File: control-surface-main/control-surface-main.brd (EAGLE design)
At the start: 105.5 x 54.1 mm, 81 parts, among them IC1 74HC595D, IC2 4051D, IC3 4051D

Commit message: in work
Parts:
- added C2, C3: (no value), rcl:C0805
- moved C1 16.9 mm to (91.4, 34.3), turned to 90 degrees
- moved K6 4.58 mm to (109.2, 12.7)
- moved KR5 4.58 mm to (109.2, 22.9)
- moved CLK_OUT 4.58 mm to (109.2, 5.08)
- moved K4 4.58 mm to (109.2, 15.2)
- moved KR7 4.58 mm to (109.2, 10.2)
- moved DAT_OUT 4.58 mm to (109.2, 7.62)
- moved K0 4.58 mm to (109.2, 20.3)
- moved K2 4.58 mm to (109.2, 17.8)
- moved K7 4.58 mm to (106.7, 12.7)
- moved KR13 4.58 mm to (106.7, 22.9)
- moved GND5 4.58 mm to (106.7, 5.08)
- moved K5 4.58 mm to (106.7, 15.2)
- moved KR6 4.58 mm to (106.7, 10.2)
- moved OE_OUT 4.58 mm to (106.7, 7.62)
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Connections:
- net GND: now also C2.2, C3.2
- net VCC: now also C2.1, C3.1
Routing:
- net DAT_IN: track 179.9 -> 142.8 mm
- net KSA: track 203.1 -> 183.3 mm
- net N$38: track 97.4 -> 85.5 mm
- net N$12: track 102.1 -> 113.9 mm
- net N$23: track 75.6 -> 64.1 mm
- net N$13: track 91.6 -> 102.1 mm
- net N$14: track 76.0 -> 85.7 mm
- net N$1: track 126.2 -> 135.4 mm
- net N$15: track 62.0 -> 71.1 mm
- net GND: track 134.6 -> 142.3 mm, vias 2 -> 5
- net N$16: track 46.0 -> 53.1 mm
- net N$19: track 116.5 -> 112.1 mm
- net N$32: track 65.5 -> 61.9 mm
- net N$35: track 63.8 -> 60.5 mm
- net N$11: track 36.1 -> 39.3 mm
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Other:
- board size 105.5 x 54.1 mm -> 102.9 x 54.1 mm

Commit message: mode mods
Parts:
- moved R7 2.54 mm to (40.6, 6.35)
- moved LED7 2.12 mm to (46.1, 5.08)
- moved R5 1.27 mm to (61.0, 6.35)
- moved LED5 0.42 mm to (66.9, 5.08)
- turned KCK to 0 degrees
- turned RD1 to 90 degrees
- renumbered ANA0 to RD0, ANA1 to KCK, CLK_IN to LCK, DAT_IN to DAT, GND to 0V, KS_CLK to RD1, OE_IN to LOE, SELA to A, SELB to B, SELC to C, VCC to 5V
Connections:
- net N$19: now also KCK.1; no longer RD1.1
- net N$45: now also RD1.1; no longer KCK.1
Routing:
- net N$45: track 51.3 -> 48.4 mm, vias 2 -> 1
- net N$31: track 33.9 -> 31.4 mm
- net VCC: track 181.4 -> 183.4 mm
- net N$29: track 55.0 -> 53.8 mm
- net N$19: track 112.1 -> 113.2 mm
- net N$24: track 4.13 -> 4.98 mm

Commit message: stuff
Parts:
- renumbered LED5 to LED3, LED6 to LED4, LED7 to LED2, LED8 to LED1, U$1 to D6, U$2 to D7, U$3 to D8, U$4 to D1, U$5 to D2, U$6 to D3, U$7 to D4, U$8 to D5
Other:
- board text added: "KEYS/LEDS"
- board text added: "POTS SCAN"

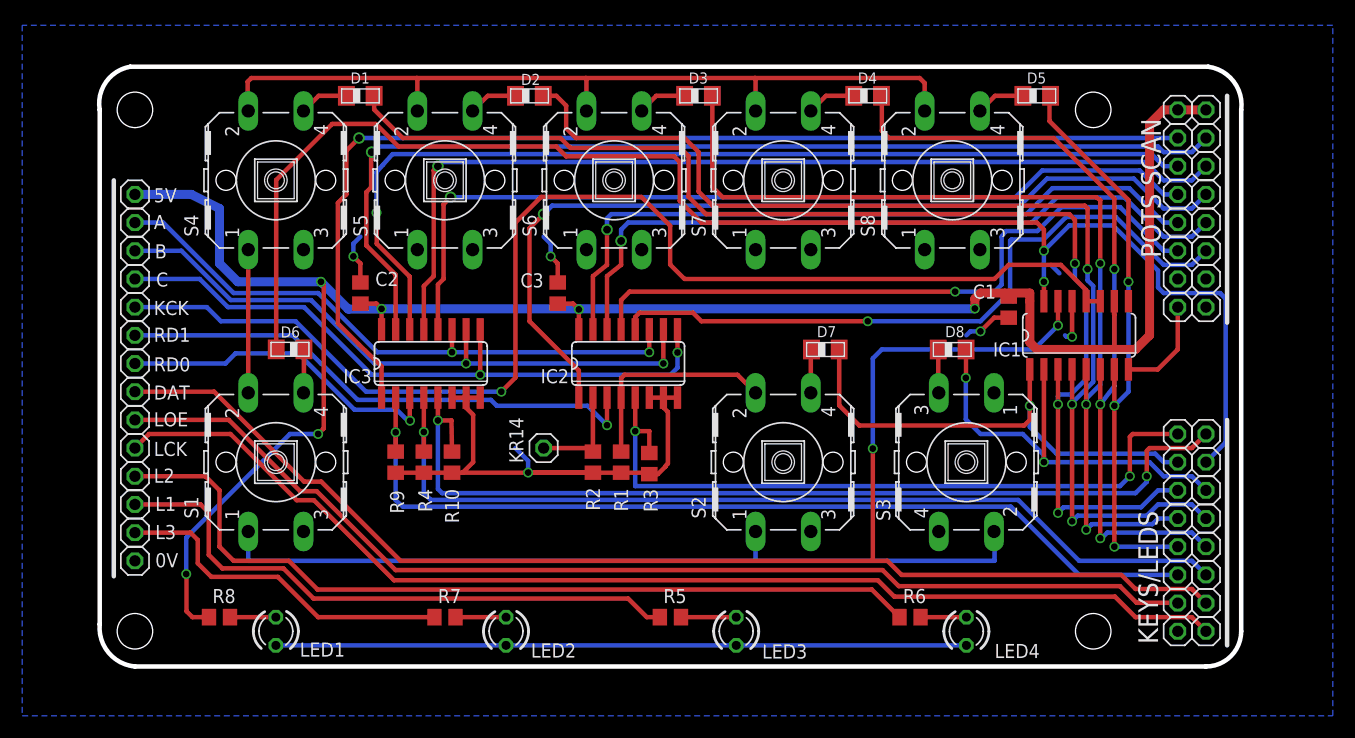
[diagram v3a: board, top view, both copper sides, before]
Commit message: move leds
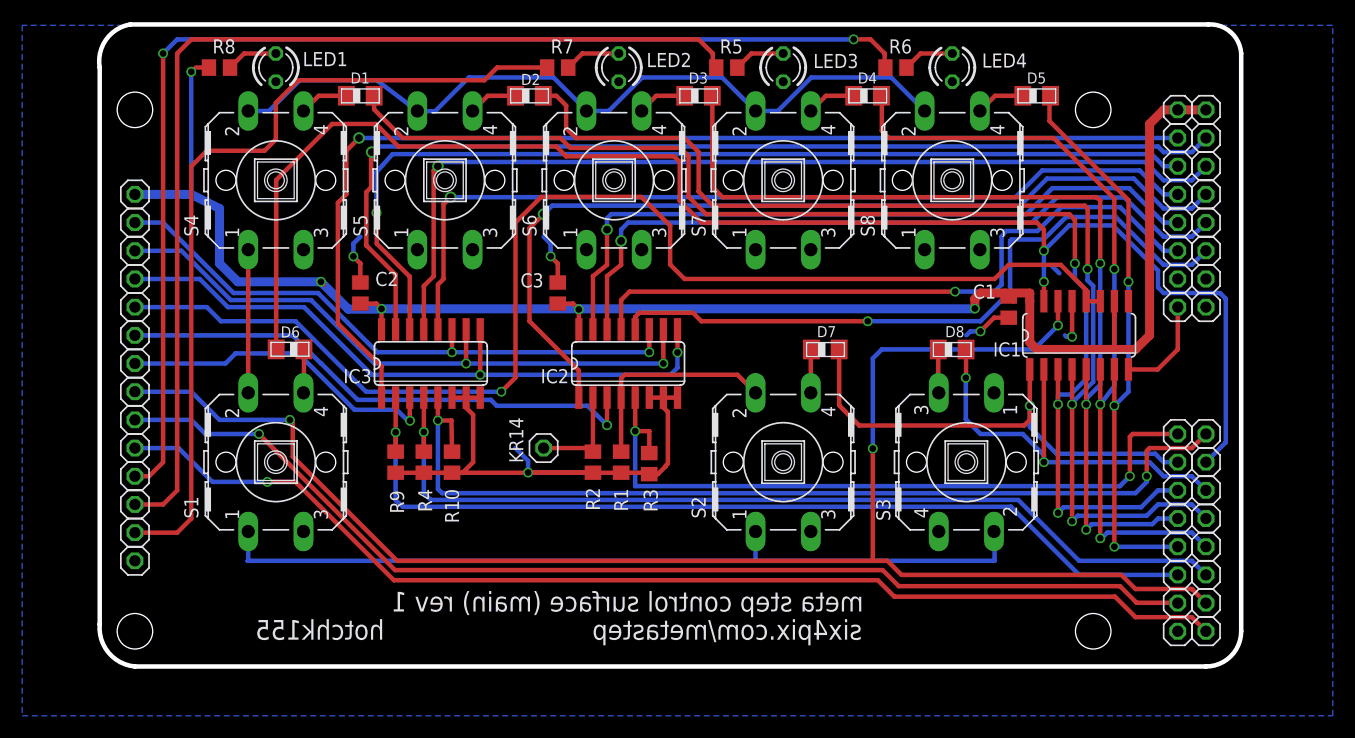
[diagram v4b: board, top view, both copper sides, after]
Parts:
- moved LED2 51.8 mm to (56.3, 55.9)
- moved LED3 51.0 mm to (71.1, 55.9)
- moved LED4 50.8 mm to (86.4, 55.9)
- moved LED1 50.8 mm to (25.4, 55.9)
- moved R7 50.6 mm to (50.8, 55.9)
- moved R5 49.8 mm to (66.0, 55.9)
- moved R6 49.5 mm to (81.3, 55.9)
- moved R8 49.5 mm to (20.3, 55.9)
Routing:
- net GND: track 142.3 -> 80.1 mm
- net N$31: track 31.4 -> 75.0 mm
- net N$29: track 53.8 -> 94.4 mm
- net N$30: track 77.1 -> 107.3 mm, vias 0 -> 2
- net VCC: track 183.4 -> 157.3 mm, vias 6 -> 5
- net KSA: track 183.2 -> 178.5 mm
- net DAT_IN: track 142.8 -> 144.5 mm, vias 2 -> 3
- net N$46: track 104.4 -> 103.4 mm, vias 0 -> 1
- net N$27: track 4.13 -> 4.66 mm
- net N$25: track 4.13 -> 4.66 mm
- net N$26: track 4.55 -> 5.08 mm
- net N$21: vias 0 -> 1
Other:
- board size 102.9 x 54.1 mm -> 102.9 x 57.9 mm
- board text added: "hotchk155"
- board text added: "meta step control surface (main) rev 1"
- board text added: "six4pix.com/metastep"
